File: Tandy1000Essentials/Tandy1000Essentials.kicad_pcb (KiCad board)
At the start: 2 copper layers, 99.9 x 99.9 mm, 23 parts, among them J1 IDE_CONNECTOR, J2 CF Adapter Power, J3 Bus_ISA_8bit, J4 Addresses, J5 Addresses, U1 BIOS FLASH, U2 74HCT245, U3 ATF/GAL22V10x-15, U4 DS1315, U5 AS6C4008-55PCN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

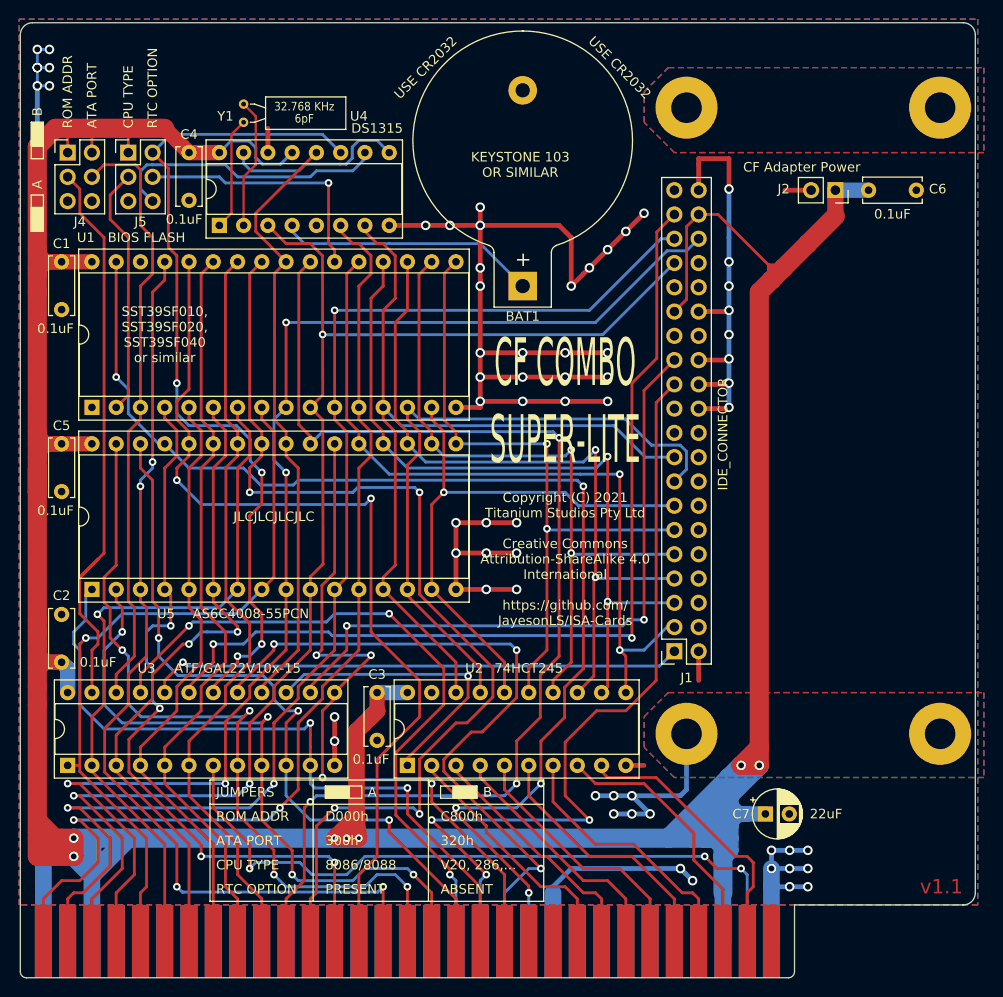
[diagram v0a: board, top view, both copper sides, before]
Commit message: Tandy 1000 Essentials: Remove references to non-Tandy 1000 configurations.
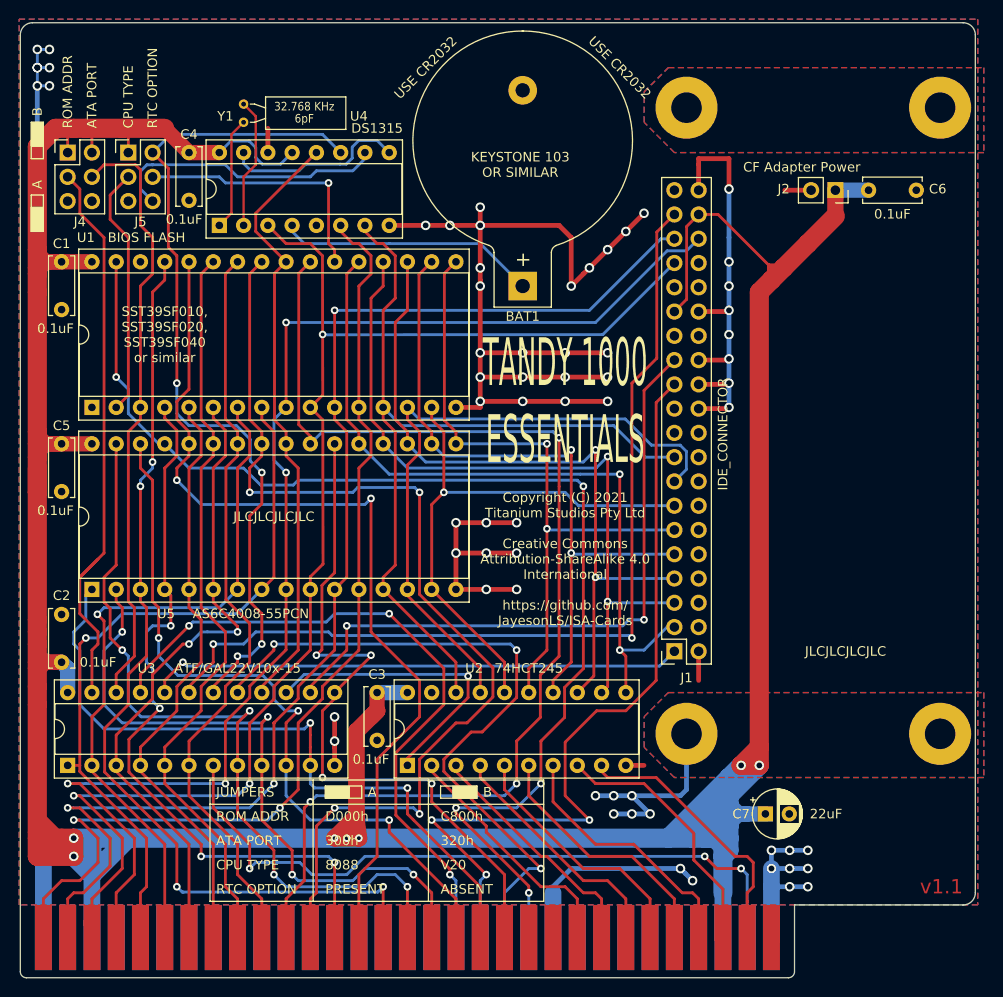
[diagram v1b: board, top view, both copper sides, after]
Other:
- board text added: "8088"
- board text added: "TANDY 1000 ESSENTIALS"
- board text added: "Thanks to the XTIDE Universal BIOS Team and others who contributed to the XTIDE Universal BIOS. Additional thanks to Rob Krenicki, Jacob Dorne/Monotech PCs, James Pearce/Lo-tech and Derek Osborn for their influencing works."
- board text added: "V20"
- board text removed: "8086/8088"
- board text removed: "CF COMBO SUPER-LITE"
- board text removed: "Compact Flash with XT-IDE BIOS"
- board text removed: "Compact Flash with XT-IDE BIOS and SmartWatch"
- board text removed: "Compact Flash with XT-IDE BIOS, SmartWatch and 512K SRAM. For original Tandy 1000, 1000A or 1000 HD only. Remove any other RAM upgrade before installing."
- board text removed: "Thanks to the XTIDE Universal BIOS Team and others who contributed to the XTIDE Universal BIOS. Additional thanks to Rob Krenicki, Jacob Dorne/Monotech PCs and James Pearce/Lo-tech for their influencing works."
- board text removed: "V20, 286,..."
